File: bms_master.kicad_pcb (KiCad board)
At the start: 4 copper layers, 85 x 65 mm, 115 parts, among them J1 Conn_01x02, J2 Conn_01x02, J3 Conn_01x02, J4 Conn_01x04, J5 Conn_01x04, J6 Conn_01x06, J7 Conn_01x05, J8 Conn_01x05, Q1 PMV15ENE, Q2 PMV74EPE, Q3 PMV74EPE, SW1 SW_Push, U1 TPS25961, U10 MAX6126, U2 TPS7B88, U3 MCP1700x-330xxMB, U4 STM32F103C8Tx, U5 TPS3851, U6 SN65HVD1050D, U7 M24C64-R, U8 741G3157, U9 MAX11163, Y1 8M

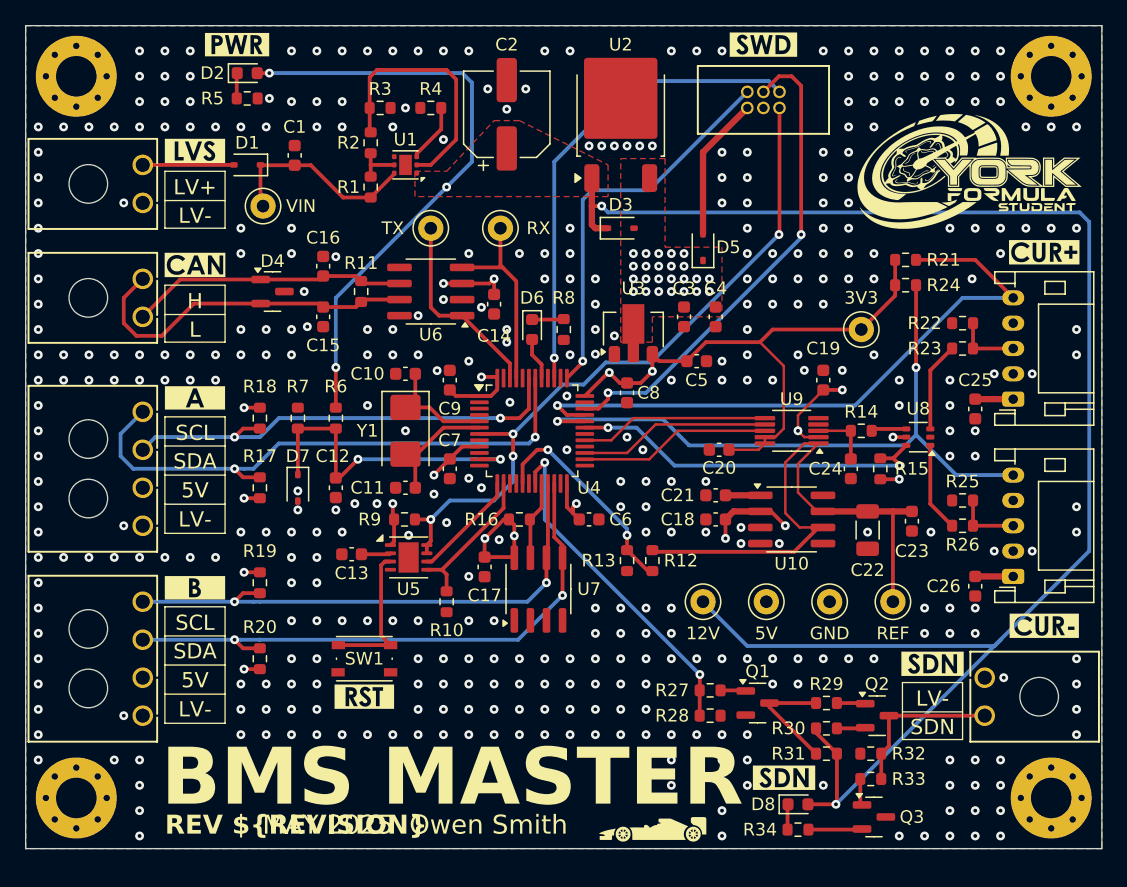
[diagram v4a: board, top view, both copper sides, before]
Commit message: pcb: Make board edge round
Also indent mounting holes to 5 mm instead of 4 mm.
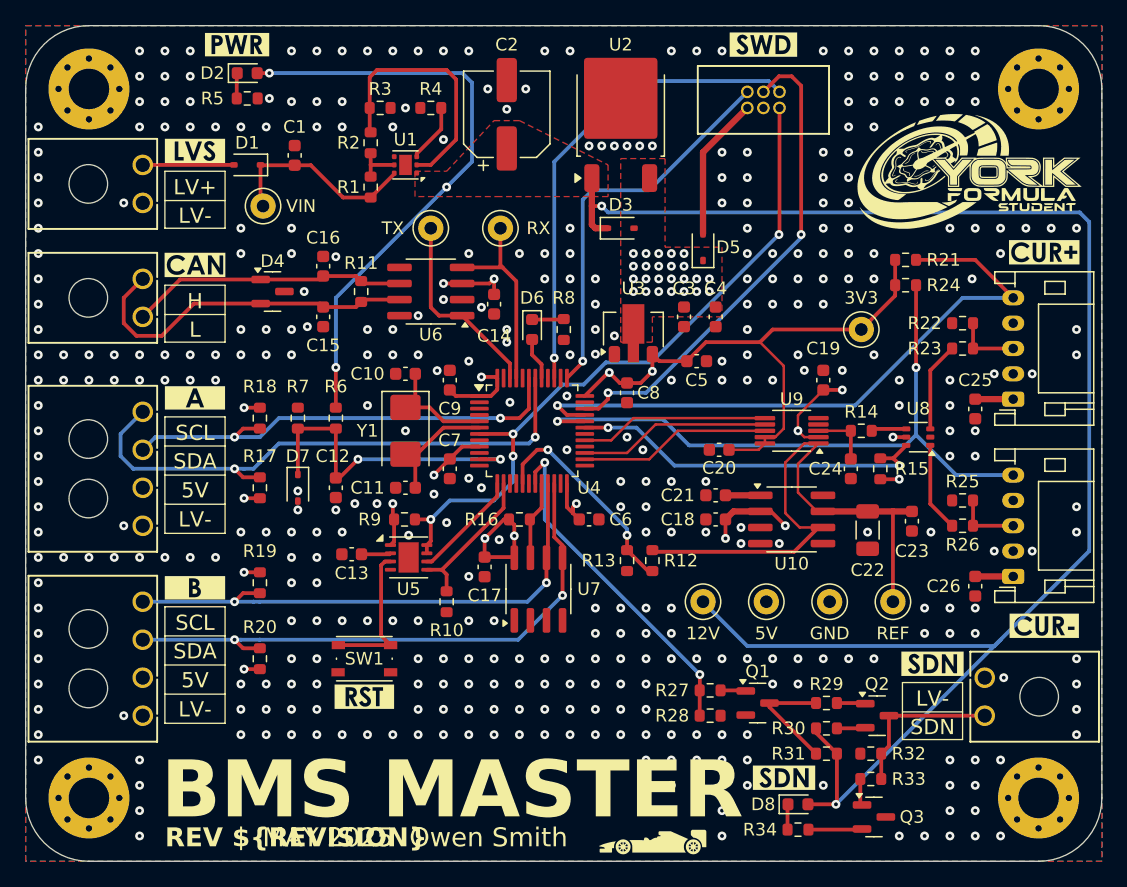
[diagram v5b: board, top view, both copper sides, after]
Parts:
- moved H1 1.41 mm to (70.0, 35.0)
- moved H3 1.41 mm to (145.0, 35.0)
- moved H2 1.00 mm to (70.0, 91.0)
- moved H4 1.00 mm to (145.0, 91.0)
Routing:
- net GND: vias 403 -> 391
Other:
- board size 85 x 65 mm -> 85 x 66 mm

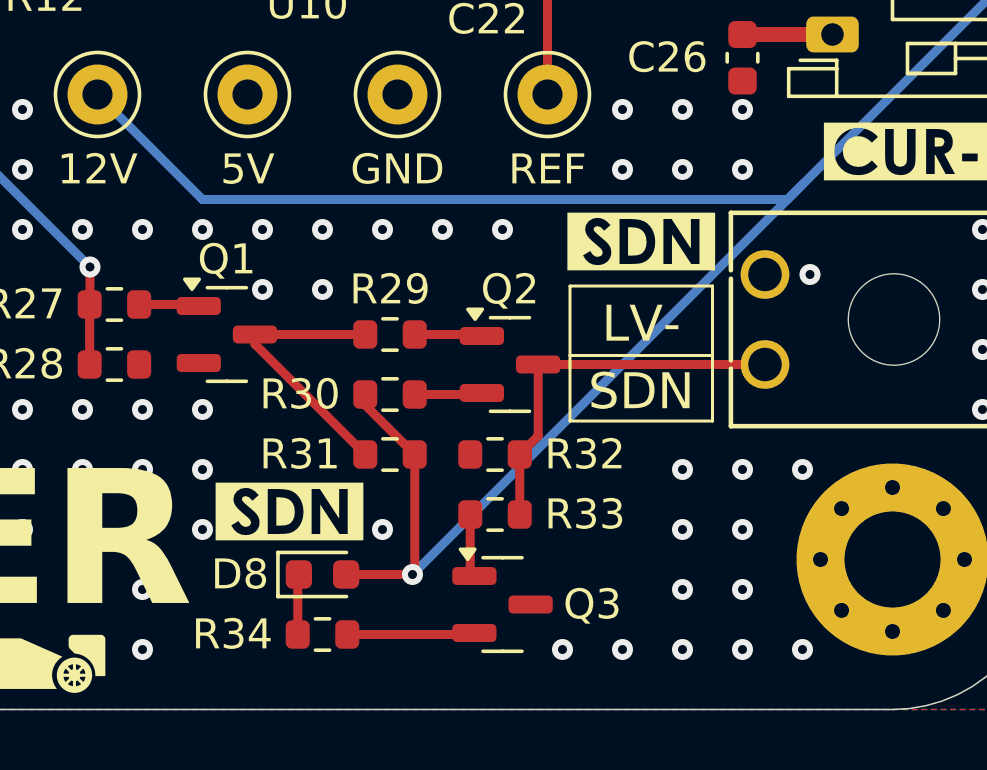
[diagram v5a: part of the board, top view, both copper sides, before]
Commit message: pcb: Move shutdown LED down slightly
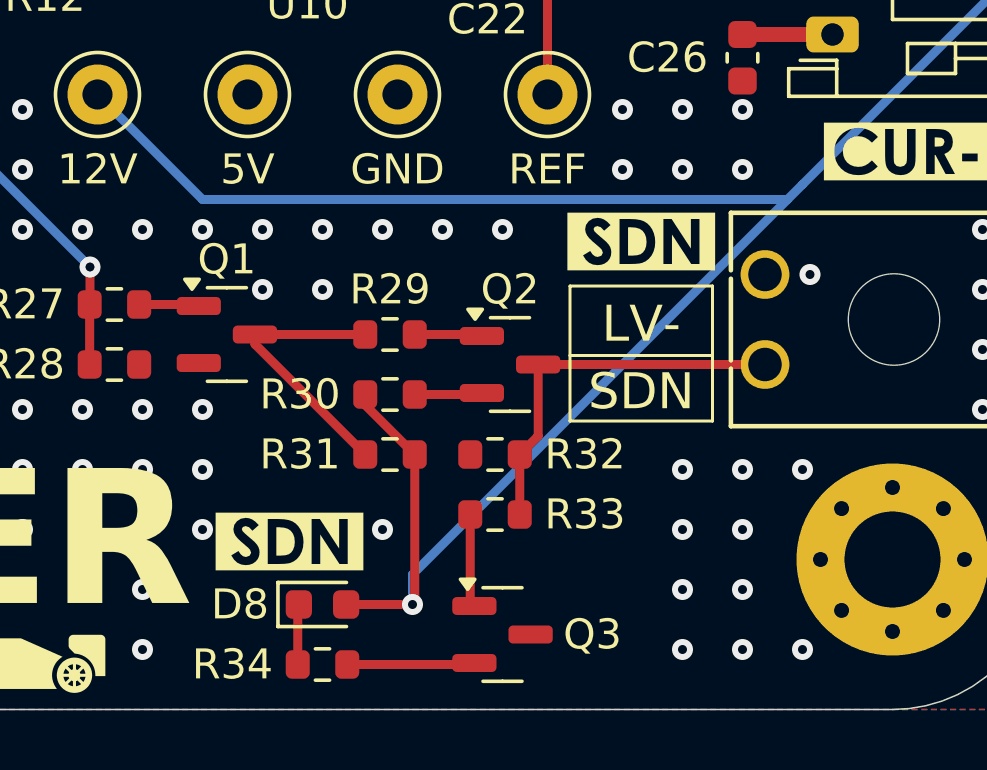
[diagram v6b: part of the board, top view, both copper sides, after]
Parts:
- moved D8 1.00 mm to (126.0, 92.5)
- moved Q3 1.00 mm to (132.0, 93.5)
- moved R34 1.00 mm to (126.0, 94.5)
- moved kibuzzard-6910B9F6 1.00 mm to (124.9, 90.4)
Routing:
- net +12V: track 180.6 -> 181.9 mm
- net Net-(Q3-G): track 2.11 -> 3.11 mm
- net GND: vias 391 -> 389
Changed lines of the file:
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@@
 	(footprint "Resistor_SMD:R_0603_1608Metric"
 		(layer "F.Cu")
-		(at 126 93.5)
+		(at 126 94.5)
 		(descr "Resistor SMD 0603 (1608 Metric), square (rectangular) end terminal, IPC-7351 nominal, (Body size source: IPC-SM-782 page 72, https://www.pcb-3d.com/wordpress/wp-content/uploads/ipc-sm-782a_amendment_1_and_2.pdf), generated with kicad-footprint-generator")
 		(tags "resistor")
@@
 	(footprint "kibuzzard-6910B9F6"
 		(layer "F.Cu")
-		(at 124.9 89.4)
+		(at 124.9 90.4)
 		(descr "Generated with KiBuzzard")
 		(tags "kb_params=eyJBbGlnbm1lbnRDaG9pY2UiOiAiQ2VudGVyIiwgIkNhcExlZnRDaG9pY2UiOiAiWyIsICJDYXBSaWdodENob2ljZSI6ICJdIiwgIkZvbnRDb21ib0JveCI6ICJjZW50dXJ5Z290aGljX2JvbGQiLCAiSGVpZ2h0Q3RybCI6IDEuNSwgIkxheWVyQ29tYm9Cb3giOiAiRi5TaWxrUyIsICJMaW5lU3BhY2luZ0N0cmwiOiAxLjUsICJNdWx0aUxpbmVUZXh0IjogIlNETiIsICJQYWRkaW5nQm90dG9tQ3RybCI6IDEuMCwgIlBhZGRpbmdMZWZ0Q3RybCI6IDMuMCwgIlBhZGRpbmdSaWdodEN0cmwiOiAzLjAsICJQYWRkaW5nVG9wQ3RybCI6IDEuMCwgIldpZHRoQ3RybCI6IDEuNSwgImFkdmFuY2VkQ2hlY2tib3giOiBmYWxzZSwgImlubGluZUZvcm1hdFRleHRib3giOiBmYWxzZSwgImxpbmVvdmVyU3R5bGVDaG9pY2UiOiAiU3F1YXJlIiwgImxpbmVvdmVyVGhpY2tuZXNzQ3RybCI6IDF9")
@@
 	(footprint "LED_SMD:LED_0603_1608Metric"
 		(layer "F.Cu")
-		(at 126 91.5)
+		(at 126 92.5)
 		(descr "LED SMD 0603 (1608 Metric), square (rectangular) end terminal, IPC-7351 nominal, (Body size source: http://www.tortai-tech.com/upload/download/2011102023233369053.pdf), generated with kicad-footprint-generator")
 		(tags "LED")
@@
 	(footprint "Package_TO_SOT_SMD:SOT-23"
 		(layer "F.Cu")
-		(at 132 92.5)
+		(at 132 93.5)
 		(descr "SOT, 3 Pin (JEDEC TO-236 Var AB https://www.jedec.org/document_search?search_api_views_fulltext=TO-236), generated with kicad-footprint-generator ipc_gullwing_generator.py")
 		(tags "SOT TO_SOT_SMD")
@@
 	)
 	(via
-		(at 134 94)
-		(size 0.7)
-		(drill 0.3)
-		(layers "F.Cu" "B.Cu")
-		(free yes)
-		(net 1)
-	)
-	(via
-		(at 136 94)
-		(size 0.7)
-		(drill 0.3)
-		(layers "F.Cu" "B.Cu")
-		(free yes)
-		(net 1)
-	)
-	(via
 		(at 128 50)
 		(size 0.7)
@@
 	)
 	(segment
-		(start 129 91.5)
-		(end 126.7875 91.5)
+		(start 129 92.5)
+		(end 126.7875 92.5)
 		(width 0.3)
 		(layer "F.Cu")
@@
 	)
 	(segment
-		(start 129.075 91.425)
-		(end 129.075 87.5)
+		(start 129.075 92.425)
+		(end 129 92.5)
 		(width 0.3)
 		(layer "F.Cu")
@@
 	)
 	(segment
+		(start 129.075 87.5)
+		(end 129.075 92.425)
+		(width 0.3)
+		(layer "F.Cu")
+		(net 13)
+	)
+	(segment
 		(start 89.5 57)
 		(end 89.5 60.175)
@@
 	)
 	(segment
-		(start 129 91.5)
-		(end 129.075 91.425)
-		(width 0.3)
-		(layer "F.Cu")
-		(net 13)
-	)
-	(segment
 		(start 129.075 87.5)
 		(end 127.425 85.85)
@@
 	)
 	(via
-		(at 129 91.5)
+		(at 129 92.5)
 		(size 0.7)
 		(drill 0.3)
@@
 	)
 	(segment
+		(start 141.5 79)
+		(end 129 91.5)
+		(width 0.3)
+		(layer "B.Cu")
+		(net 13)
+	)
+	(segment
 		(start 149 45.5)
 		(end 149 71.5)
@@
 	)
 	(segment
-		(start 142 78.5)
-		(end 129 91.5)
+		(start 129 91.5)
+		(end 129 92.5)
 		(width 0.3)
 		(layer "B.Cu")
@@
 	)
 	(segment
-		(start 125.25 91.4625)
-		(end 125.2125 91.5)
+		(start 125.25 92.4625)
+		(end 125.2125 92.5)
 		(width 0.3)
 		(layer "F.Cu")
@@
 	)
 	(segment
-		(start 125.175 91.5375)
-		(end 125.2125 91.5)
+		(start 125.175 92.5375)
+		(end 125.2125 92.5)
 		(width 0.3)
 		(layer "F.Cu")
@@
 	)
 	(segment
-		(start 125.175 93.5)
-		(end 125.175 91.5375)
+		(start 125.175 94.5)
+		(end 125.175 92.5375)
 		(width 0.3)
 		(layer "F.Cu")
@@
 	)
 	(segment
-		(start 130.925 91.4125)
-		(end 131.0625 91.55)
+		(start 130.925 92.4125)
+		(end 130.925 89.5)
 		(width 0.3)
 		(layer "F.Cu")
@@
 	)
 	(segment
-		(start 130.925 89.5)
-		(end 130.925 91.4125)
+		(start 131.0625 92.55)
+		(end 130.925 92.4125)
 		(width 0.3)
 		(layer "F.Cu")
@@
 	)
 	(segment
-		(start 126.825 93.5)
-		(end 131.0125 93.5)
+		(start 126.825 94.5)
+		(end 131.0125 94.5)
 		(width 0.3)
 		(layer "F.Cu")
@@
 	)
 	(segment
-		(start 131.0125 93.5)
-		(end 131.0625 93.45)
+		(start 131.0125 94.5)
+		(end 131.0625 94.45)
 		(width 0.3)
 		(layer "F.Cu")
